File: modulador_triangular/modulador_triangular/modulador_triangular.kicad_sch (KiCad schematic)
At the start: 12 parts, among them J1 OUT, J2 V1_12, J3 SIN, U1 LM7806_TO220, U1_2 ADTL082, U3 LT1016, U4 ADTL082

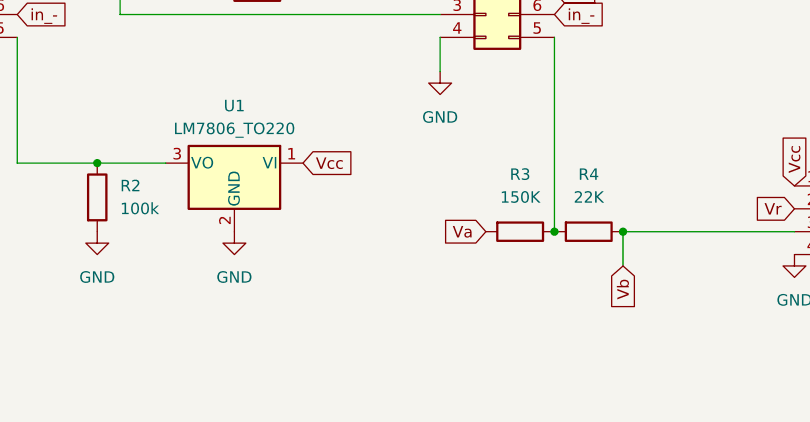
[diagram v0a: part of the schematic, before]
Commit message: pcb del pwm
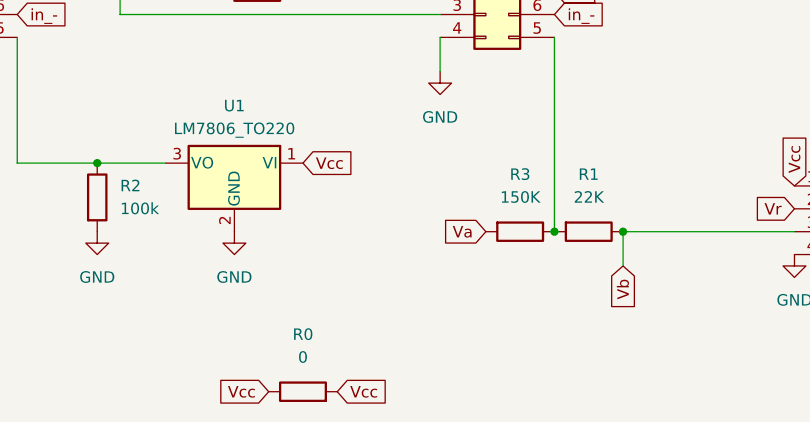
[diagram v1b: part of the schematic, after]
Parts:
- removed R4: 22K, Resistor_THT:R_Axial_DIN0204_L3.6mm_D1.6mm_P7.62mm_Horizontal, symbol Device:R
- added R0: 0, Resistor_THT:R_Axial_DIN0207_L6.3mm_D2.5mm_P10.16mm_Horizontal, symbol Device:R
- added R1: 22K, Resistor_THT:R_Axial_DIN0204_L3.6mm_D1.6mm_P7.62mm_Horizontal, symbol Device:R
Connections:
- net Vb: now also R1.1
- net Vcc: now also R0.1, R0.2
- net at R3.1, U1_2.5 (Pin_5): now also R1.2
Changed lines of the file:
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@@
 	(paper "A4")
+	(junction
+		(at 74.93 132.08)
+		(diameter 0)
+		(color 0 0 0 0)
+	)
+	(junction
+		(at 99.06 113.03)
+		(diameter 0)
+		(color 0 0 0 0)
+	)
+	(junction
+		(at 133.35 139.7)
+		(diameter 0)
+		(color 0 0 0 0)
+	)
 	(junction
 		(at 125.73 139.7)
@@
 		(color 0 0 0 0)
 	)
-	(junction
-		(at 74.93 132.08)
-		(diameter 0)
-		(color 0 0 0 0)
-	)
-	(junction
-		(at 99.06 113.03)
-		(diameter 0)
-		(color 0 0 0 0)
-	)
-	(junction
-		(at 133.35 139.7)
-		(diameter 0)
-		(color 0 0 0 0)
-	)
 	(wire
 		(pts
@@
 		)
 	)
+	(global_label "Vcc"
+		(shape input)
+		(at 101.6 157.48 0)
+		(fields_autoplaced yes)
+		(effects
+			(font
+				(size 1.27 1.27)
+			)
+			(justify left)
+		)
+		(property "Intersheetrefs" "${INTERSHEET_REFS}"
+			(at 107.851 157.48 0)
+			(effects
+				(font
+					(size 1.27 1.27)
+				)
+				(justify left)
+				(hide yes)
+			)
+		)
+	)
 	(global_label "Va"
 		(shape input)
@@
 		)
 	)
+	(global_label "Vcc"
+		(shape input)
+		(at 93.98 157.48 180)
+		(fields_autoplaced yes)
+		(effects
+			(font
+				(size 1.27 1.27)
+			)
+			(justify right)
+		)
+		(property "Intersheetrefs" "${INTERSHEET_REFS}"
+			(at 87.729 157.48 0)
+			(effects
+				(font
+					(size 1.27 1.27)
+				)
+				(justify right)
+				(hide yes)
+			)
+		)
+	)
 	(global_label "Vr"
 		(shape input)
@@
 	)
 	(symbol
+		(lib_id "Device:R")
+		(at 129.54 139.7 270)
+		(unit 1)
+		(exclude_from_sim no)
+		(in_bom yes)
+		(on_board yes)
+		(dnp no)
+		(fields_autoplaced yes)
+		(property "Reference" "R1"
+			(at 129.54 133.35 90)
+			(effects
+				(font
+					(size 1.27 1.27)
+				)
+			)
+		)
+		(property "Value" "22K"
+			(at 129.54 135.89 90)
+			(effects
+				(font
+					(size 1.27 1.27)
+				)
+			)
+		)
+		(property "Footprint" "Resistor_THT:R_Axial_DIN0204_L3.6mm_D1.6mm_P7.62mm_Horizontal"
+			(at 129.54 137.922 90)
+			(effects
+				(font
+					(size 1.27 1.27)
+				)
+				(hide yes)
+			)
+		)
+		(property "Datasheet" "~"
+			(at 129.54 139.7 0)
+			(effects
+				(font
+					(size 1.27 1.27)
+				)
+				(hide yes)
+			)
+		)
+		(property "Description" "Resistor"
+			(at 129.54 139.7 0)
+			(effects
+				(font
+					(size 1.27 1.27)
+				)
+				(hide yes)
+			)
+		)
+		(pin "2"
+		)
+		(pin "1"
+		)
+		(instances
+			(project "modulador_triangular"
+				(path "/2b400cfa-efc2-4e32-b6b6-fe8ff679fa68"
+					(reference "R1")
+					(unit 1)
+				)
+			)
+		)
+	)
+	(symbol
 		(lib_id "power:GND")
 		(at 152.4 142.24 0)
@@
 	)
 	(symbol
-		(lib_id "Device:R")
-		(at 129.54 139.7 270)
-		(unit 1)
-		(exclude_from_sim no)
-		(in_bom yes)
-		(on_board yes)
-		(dnp no)
-		(fields_autoplaced yes)
-		(property "Reference" "R4"
-			(at 129.54 133.35 90)
-			(effects
-				(font
-					(size 1.27 1.27)
-				)
-			)
-		)
-		(property "Value" "22K"
-			(at 129.54 135.89 90)
-			(effects
-				(font
-					(size 1.27 1.27)
-				)
-			)
-		)
-		(property "Footprint" "Resistor_THT:R_Axial_DIN0204_L3.6mm_D1.6mm_P7.62mm_Horizontal"
-			(at 129.54 137.922 90)
-			(effects
-				(font
-					(size 1.27 1.27)
-				)
-				(hide yes)
-			)
-		)
-		(property "Datasheet" "~"
-			(at 129.54 139.7 0)
-			(effects
-				(font
-					(size 1.27 1.27)
-				)
-				(hide yes)
-			)
-		)
-		(property "Description" "Resistor"
-			(at 129.54 139.7 0)
-			(effects
-				(font
-					(size 1.27 1.27)
-				)
-				(hide yes)
-			)
-		)
-		(pin "2"
-		)
-		(pin "1"
-		)
-		(instances
-			(project "modulador_triangular"
-				(path "/2b400cfa-efc2-4e32-b6b6-fe8ff679fa68"
-					(reference "R4")
-					(unit 1)
-				)
-			)
-		)
-	)
-	(symbol
 		(lib_id "Connector:Conn_01x02_Socket")
 		(at 99.06 83.82 0)
@@
 					(unit 1)
 				)
+			)
+		)
+	)
+	(symbol
+		(lib_id "Device:R")
+		(at 97.79 157.48 90)
+		(unit 1)
+		(exclude_from_sim no)
+		(in_bom yes)
+		(on_board yes)
+		(dnp no)
+		(fields_autoplaced yes)
+		(property "Reference" "R0"
+			(at 97.79 151.13 90)
+			(effects
+				(font
+					(size 1.27 1.27)
+				)
+			)
+		)
+		(property "Value" "0"
+			(at 97.79 153.67 90)
+			(effects
+				(font
+					(size 1.27 1.27)
+				)
+			)
+		)
+		(property "Footprint" "Resistor_THT:R_Axial_DIN0207_L6.3mm_D2.5mm_P10.16mm_Horizontal"
+			(at 97.79 159.258 90)
+			(effects
+				(font
+					(size 1.27 1.27)
+				)
+				(hide yes)
+			)
+		)
+		(property "Datasheet" "~"
+			(at 97.79 157.48 0)
+			(effects
+				(font
+					(size 1.27 1.27)
+				)
+				(hide yes)
+			)
+		)
+		(property "Description" "Resistor"
+			(at 97.79 157.48 0)
+			(effects
+				(font
+					(size 1.27 1.27)
+				)
+				(hide yes)
+			)
+		)
+		(pin "2"
+		)
+		(pin "1"
+		)
+		(instances
+			(project "modulador_triangular"
+				(path "/2b400cfa-efc2-4e32-b6b6-fe8ff679fa68"
+					(reference "R0")
+					(unit 1)
+				)

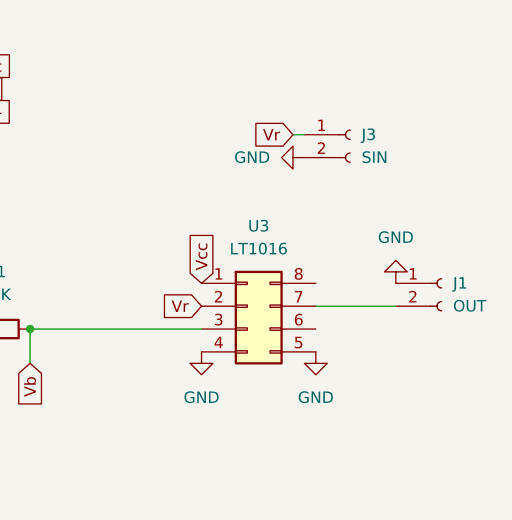
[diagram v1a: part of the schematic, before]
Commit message: pcb del pwm
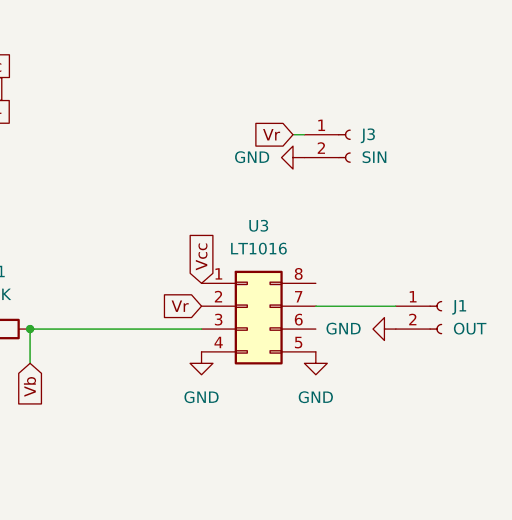
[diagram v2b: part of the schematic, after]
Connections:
- net GND: now also J1.2 (Pin_2); no longer J1.1 (Pin_1)
- net at U3.7 (Pin_7): now also J1.1 (Pin_1); no longer J1.2 (Pin_2)
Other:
- moved on the sheet: J1
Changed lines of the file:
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@@
+	(wire
+		(pts
+			(xy 165.1 137.16) (xy 173.99 137.16)
+		)
+		(stroke
+			(width 0)
+			(type default)
+		)
+	)
 	(wire
 		(pts
@@
 		(pts
 			(xy 85.09 109.22) (xy 85.09 113.03)
-		)
-		(stroke
-			(width 0)
-			(type default)
-		)
-	)
-	(wire
-		(pts
-			(xy 173.99 137.16) (xy 165.1 137.16)
 		)
 		(stroke
@@
 				(path "/2b400cfa-efc2-4e32-b6b6-fe8ff679fa68"
 					(reference "U4")
-					(unit 1)
-				)
-			)
-		)
-	)
-	(symbol
-		(lib_id "power:GND")
-		(at 173.99 134.62 180)
-		(unit 1)
-		(exclude_from_sim no)
-		(in_bom yes)
-		(on_board yes)
-		(dnp no)
-		(fields_autoplaced yes)
-		(property "Reference" "#PWR06"
-			(at 173.99 128.27 0)
-			(effects
-				(font
-					(size 1.27 1.27)
-				)
-				(hide yes)
-			)
-		)
-		(property "Value" "GND"
-			(at 173.99 129.54 0)
-			(effects
-				(font
-					(size 1.27 1.27)
-				)
-			)
-		)
-		(property "Footprint" ""
-			(at 173.99 134.62 0)
-			(effects
-				(font
-					(size 1.27 1.27)
-				)
-				(hide yes)
-			)
-		)
-		(property "Datasheet" ""
-			(at 173.99 134.62 0)
-			(effects
-				(font
-					(size 1.27 1.27)
-				)
-				(hide yes)
-			)
-		)
-		(property "Description" "Power symbol creates a global label with name \"GND\" , ground"
-			(at 173.99 134.62 0)
-			(effects
-				(font
-					(size 1.27 1.27)
-				)
-				(hide yes)
-			)
-		)
-		(pin "1"
-		)
-		(instances
-			(project "modulador_triangular"
-				(path "/2b400cfa-efc2-4e32-b6b6-fe8ff679fa68"
-					(reference "#PWR06")
 					(unit 1)
 				)
@@
 	(symbol
 		(lib_id "power:GND")
+		(at 173.99 139.7 270)
+		(unit 1)
+		(exclude_from_sim no)
+		(in_bom yes)
+		(on_board yes)
+		(dnp no)
+		(fields_autoplaced yes)
+		(property "Reference" "#PWR06"
+			(at 167.64 139.7 0)
+			(effects
+				(font
+					(size 1.27 1.27)
+				)
+				(hide yes)
+			)
+		)
+		(property "Value" "GND"
+			(at 170.18 139.6999 90)
+			(effects
+				(font
+					(size 1.27 1.27)
+				)
+				(justify right)
+			)
+		)
+		(property "Footprint" ""
+			(at 173.99 139.7 0)
+			(effects
+				(font
+					(size 1.27 1.27)
+				)
+				(hide yes)
+			)
+		)
+		(property "Datasheet" ""
+			(at 173.99 139.7 0)
+			(effects
+				(font
+					(size 1.27 1.27)
+				)
+				(hide yes)
+			)
+		)
+		(property "Description" "Power symbol creates a global label with name \"GND\" , ground"
+			(at 173.99 139.7 0)
+			(effects
+				(font
+					(size 1.27 1.27)
+				)
+				(hide yes)
+			)
+		)
+		(pin "1"
+		)
+		(instances
+			(project "modulador_triangular"
+				(path "/2b400cfa-efc2-4e32-b6b6-fe8ff679fa68"
+					(reference "#PWR06")
+					(unit 1)
+				)
+			)
+		)
+	)
+	(symbol
+		(lib_id "power:GND")
 		(at 163.83 120.65 270)
 		(unit 1)
@@
 	(symbol
 		(lib_id "Connector:Conn_01x02_Socket")
-		(at 179.07 134.62 0)
+		(at 179.07 137.16 0)
 		(unit 1)
 		(exclude_from_sim no)
@@
 		(fields_autoplaced yes)
 		(property "Reference" "J1"
-			(at 180.34 134.6199 0)
+			(at 180.34 137.1599 0)
 			(effects
 				(font
@@
 		)
 		(property "Value" "OUT"
-			(at 180.34 137.1599 0)
+			(at 180.34 139.6999 0)
 			(effects
 				(font
@@
 		)
 		(property "Footprint" "TerminalBlock_Phoenix:TerminalBlock_Phoenix_MKDS-3-2-5.08_1x02_P5.08mm_Horizontal"
-			(at 179.07 134.62 0)
+			(at 179.07 137.16 0)
 			(effects
 				(font
@@
 		)
 		(property "Datasheet" "~"
-			(at 179.07 134.62 0)
+			(at 179.07 137.16 0)
 			(effects
 				(font
@@
 		)
 		(property "Description" "Generic connector, single row, 01x02, script generated"
-			(at 179.07 134.62 0)
-			(effects
-				(font
+			(at 179.07 137.16 0)
+			(effects
+				(font

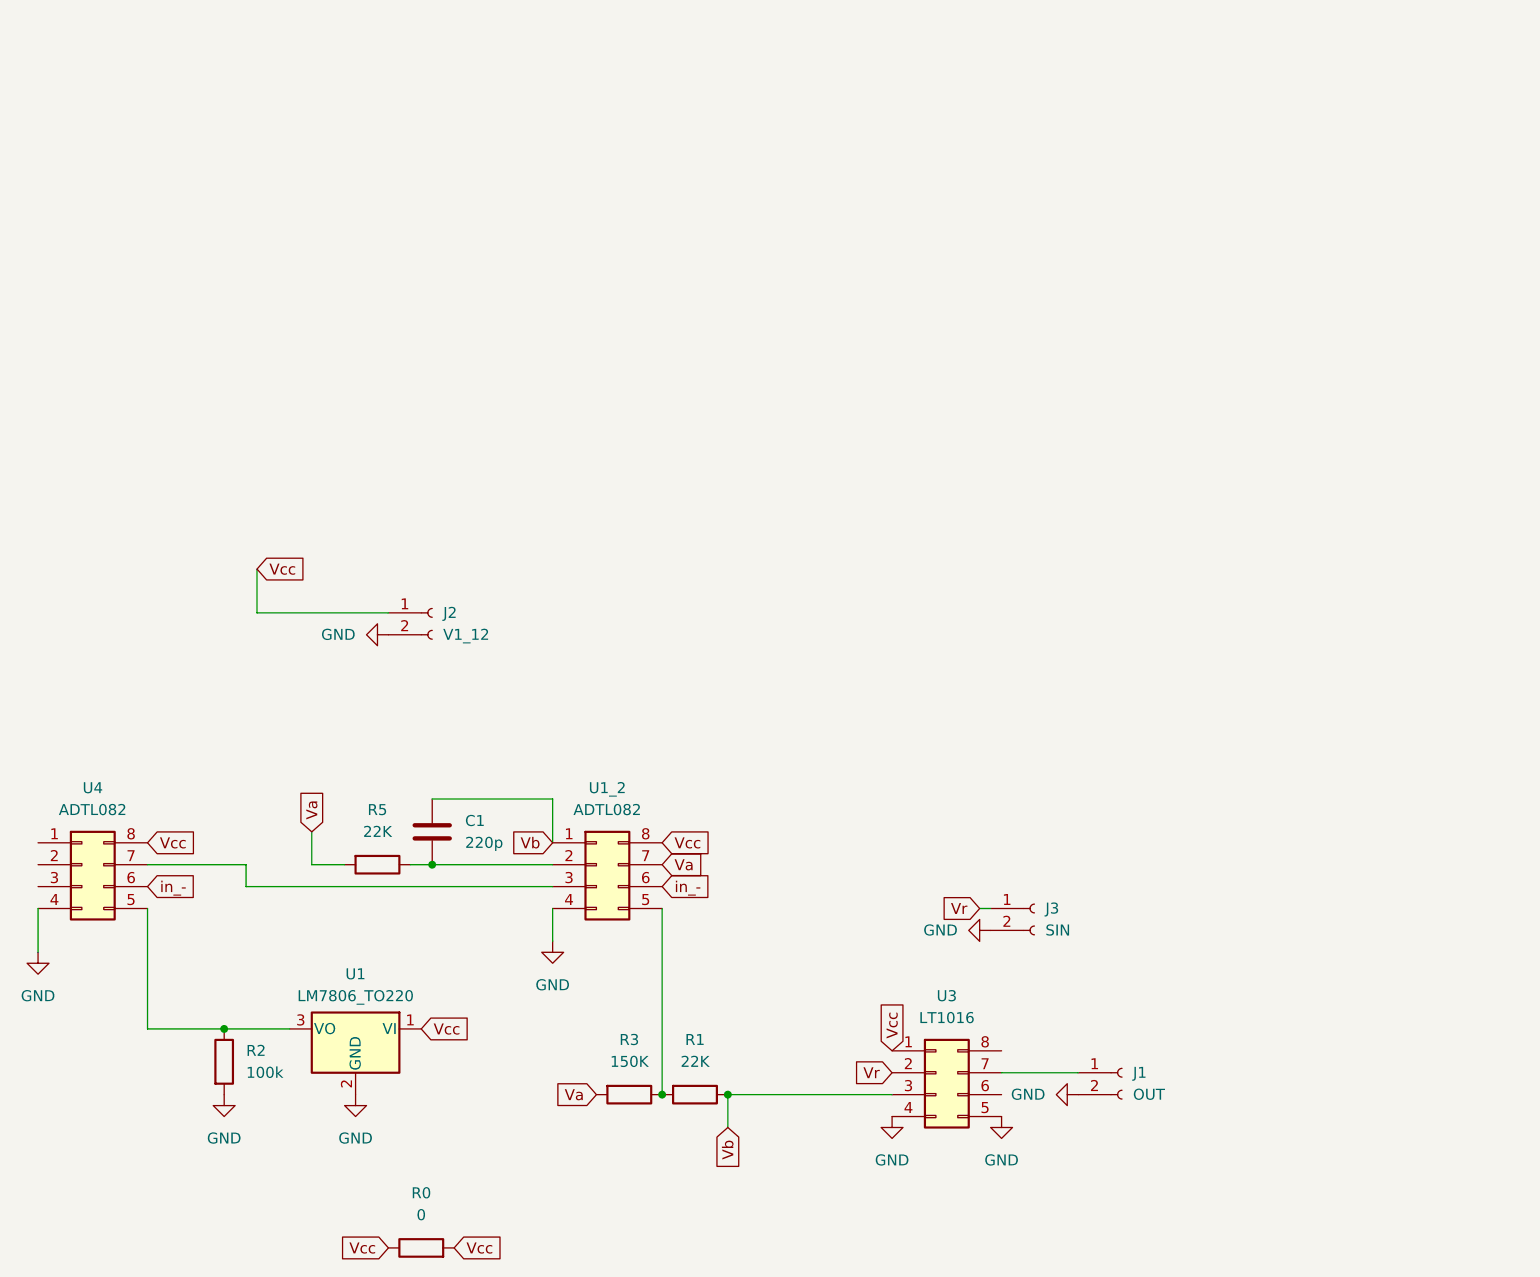
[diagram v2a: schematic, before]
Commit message: modificaciones de pcb del pwm
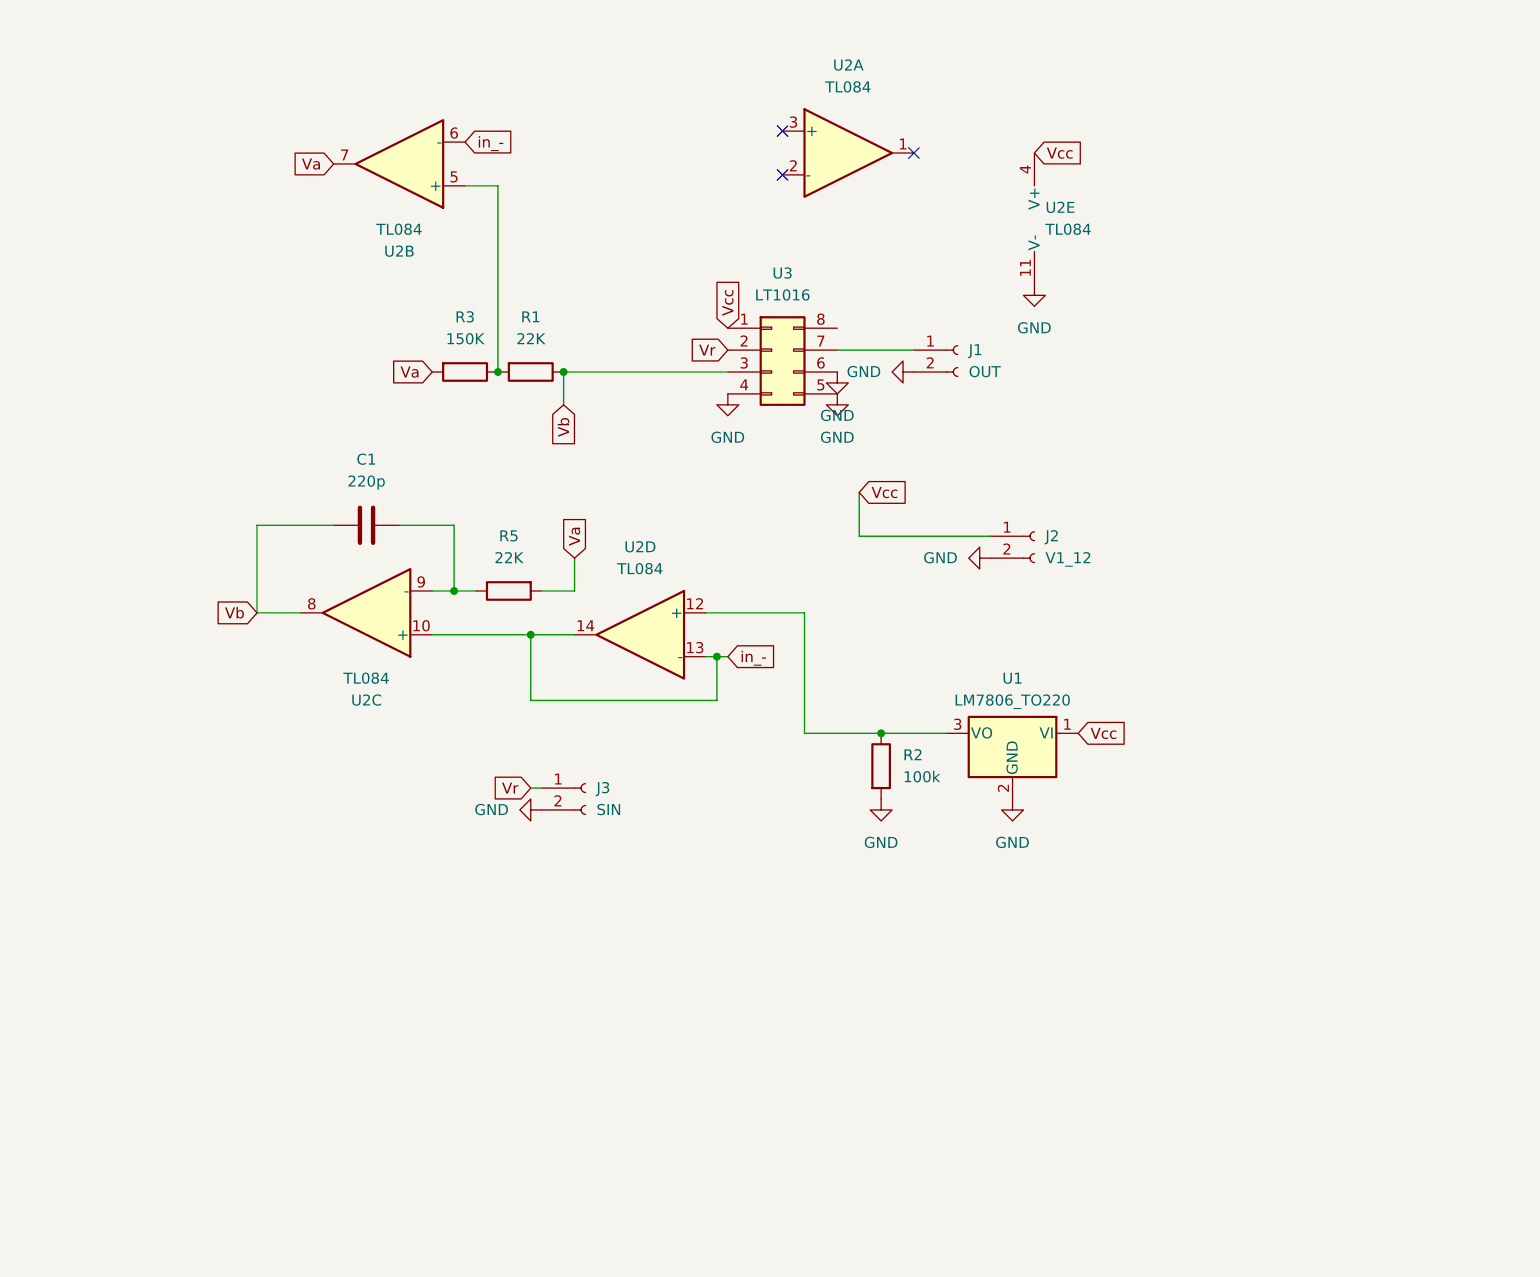
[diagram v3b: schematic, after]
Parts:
- removed R0: 0, Resistor_THT:R_Axial_DIN0207_L6.3mm_D2.5mm_P10.16mm_Horizontal, symbol Device:R
- removed U1_2, U4: ADTL082, Package_DIP:DIP-8_W7.62mm, symbol Connector_Generic:Conn_02x04_Counter_Clockwise
- added U2: TL084, Package_DIP:DIP-14_W7.62mm_Socket_LongPads, symbol Amplifier_Operational:TL084
- R1, R2, R3, R5: footprint Resistor_THT:R_Axial_DIN0204_L3.6mm_D1.6mm_P7.62mm_Horizontal -> Resistor_THT:R_Axial_DIN0207_L6.3mm_D2.5mm_P7.62mm_Horizontal
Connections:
- net GND: now also U3.6 (Pin_6), U2.11 (V-)
- net Va: now also U2.7
- net Vb: now also U2.8
- net Vcc: now also U2.4 (V+)
- net in_-: now also U2.10 (+), U2.13 (-), U2.14, U2.6 (-)
- net at R2.1, U1.3 (VO): now also U2.12 (+)
- net at R1.2, R3.1: now also U2.5 (+)
- net at C1.1, R5.1: now also U2.9 (-)
- no-connect marks 0 -> 3
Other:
- moved on the sheet: C1, J1, J2, J3, R1, R2, R3, R5, U1, U3

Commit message: modificaciones en la support
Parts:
- removed U2: TL084, Package_DIP:DIP-14_W7.62mm_Socket_LongPads, symbol Amplifier_Operational:TL084
- removed U3: LT1016, Package_DIP:DIP-8_W7.62mm, symbol Connector_Generic:Conn_02x04_Counter_Clockwise
- added C2: 0.1u, Capacitor_THT:C_Disc_D5.0mm_W2.5mm_P5.00mm, symbol Device:C
- added C3: 0.33u, Capacitor_THT:C_Disc_D5.0mm_W2.5mm_P5.00mm, symbol Device:C
- added R4: 10k, Resistor_THT:R_Axial_DIN0207_L6.3mm_D2.5mm_P7.62mm_Horizontal, symbol Device:R
- added R6: 1k, Resistor_THT:R_Axial_DIN0207_L6.3mm_D2.5mm_P7.62mm_Horizontal, symbol Device:R
- added U4: TL082, Package_DIP:DIP-8_W7.62mm_LongPads, symbol Amplifier_Operational:TL082
- added U5: LM393, Package_DIP:DIP-8_W7.62mm_LongPads, symbol Comparator:LM393
- C1: value 220p -> 470p
- R1: value 22K -> 100K
- R3: value 150K -> 390K
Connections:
- net GND: now also C2.2, C3.2, U4.4 (V-), U5.4 (V-)
- net Va: now also R6.2, U5.1
- net Vb: now also U4.1, U5.6 (-)
- net Vcc: now also C3.1, R4.1, R6.1, U4.8 (V+), U5.8 (V+)
- net Vr: now also U5.5 (+)
- net in_-: now also U4.3 (+), U4.6 (-), U4.7, U5.2 (-)
- net at R2.1, U1.3 (VO): now also C2.1, U4.5 (+)
- net at J1.1 (Pin_1): now also R4.2, U5.7
- net at C1.1, R5.1: now also U4.2 (-)
- net at R1.2, R3.1: now also U5.3 (+)
- no-connect marks 3 -> 0
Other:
- moved on the sheet: R2
